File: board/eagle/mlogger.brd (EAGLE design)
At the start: 59.4 x 33.3 mm, 47 parts, among them J1 MICROSD-9P, SW1 SS-12D00G3, SW2 TVAF06-A020B-R, SW3 TVAF06-A020B-R

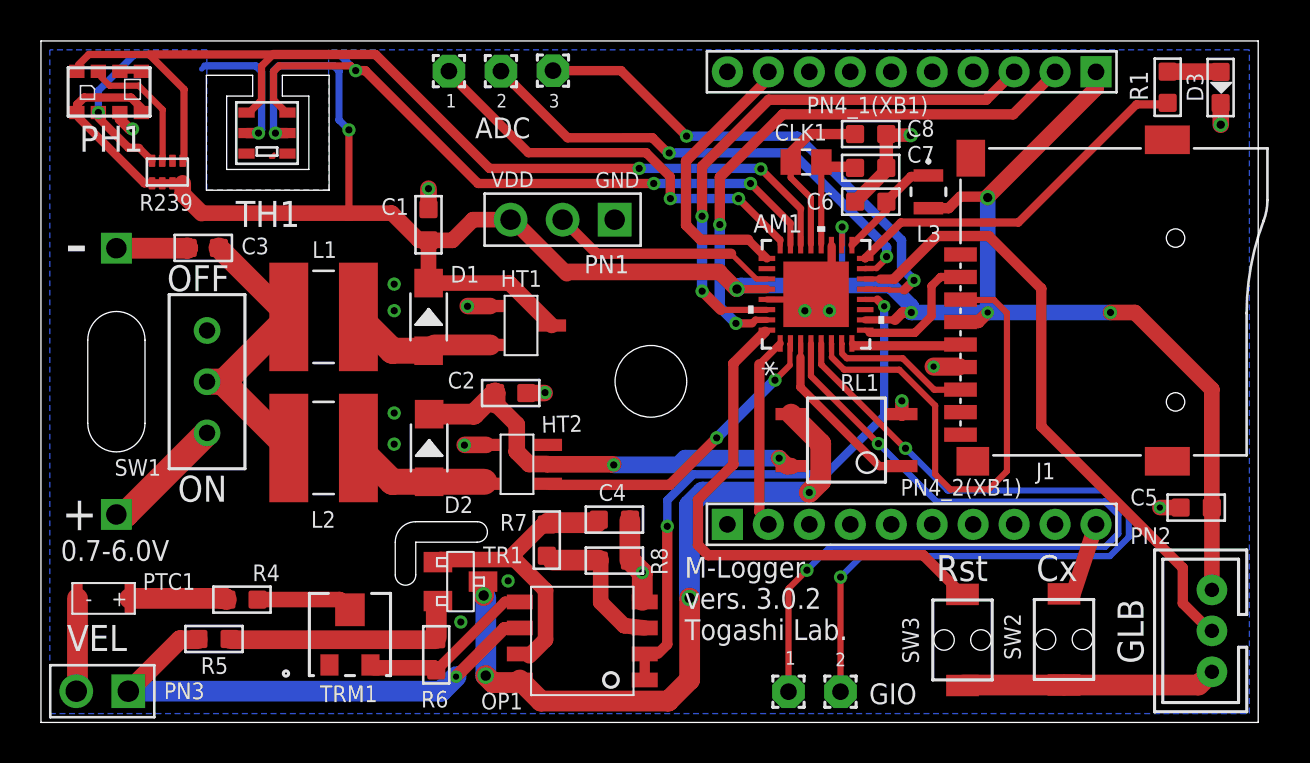
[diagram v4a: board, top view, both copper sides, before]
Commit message: 風速計配線ルート改善
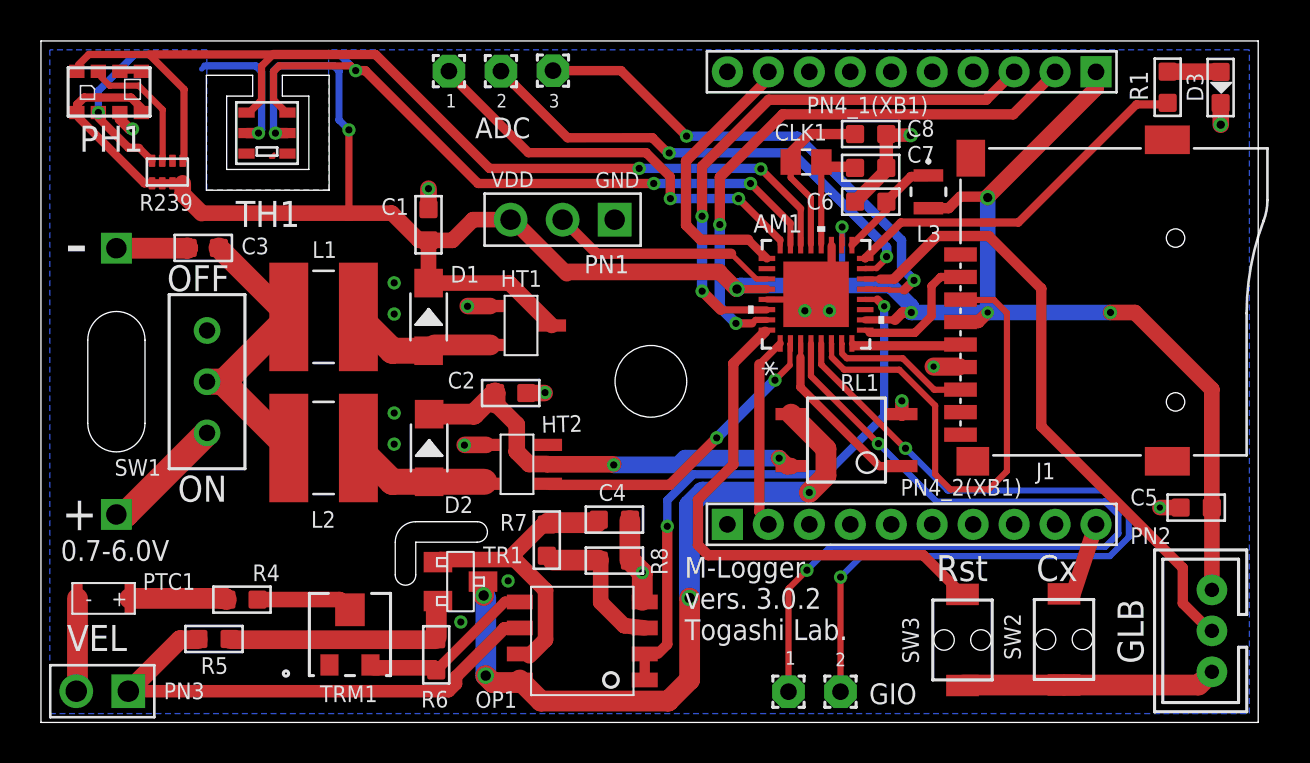
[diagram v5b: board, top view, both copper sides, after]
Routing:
- net P$1: track 24.9 -> 25.1 mm, vias 1 -> 0
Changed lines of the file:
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@@
 <element name="D2" library="Seeed-Diode" package="SOD-123" value="20V-1A" x="18.9546" y="13.4" smashed="yes" rot="R90">
 <attribute name="MPN" value="B5819W" x="18.9546" y="13.4" size="1.778" layer="27" rot="R90" display="off"/>
+<attribute name="NAME" x="19.5896" y="12.511" size="0.381" layer="33" ratio="10" rot="R90"/>
 <attribute name="NAME" x="19.6864" y="10.2246" size="0.8128" layer="25" ratio="11"/>
-<attribute name="NAME" x="19.5896" y="12.511" size="0.381" layer="33" ratio="10" rot="R90"/>
 <attribute name="VALUE" x="20.9866" y="11.495" size="0.889" layer="27" font="vector" ratio="11" rot="R90"/>
 </element>
@@
 </element>
 <element name="OP1" library="MyParts" package="NJM4565" value="NJM4565" x="29.4814" y="2.0724" smashed="yes" rot="R90">
-<attribute name="NAME" x="21.4874" y="0.6356" size="0.8128" layer="25"/>
+<attribute name="NAME" x="21.208" y="0.7118" size="0.8128" layer="25"/>
 </element>
 <element name="PTC1" library="MyParts" package="TFPT1206" value="TFPT1206" x="1.7832" y="6.055" smashed="yes">
@@
 <via x="22.8092" y="6.9088" extent="1-16" drill="0.35"/>
 <via x="17.2466" y="13.5866" extent="1-16" drill="0.35"/>
-<via x="17.2466" y="20.1042" extent="1-16" drill="0.35"/>
-<via x="17.2466" y="21.4004" extent="1-16" drill="0.35"/>
+<via x="17.2466" y="19.939" extent="1-16" drill="0.35"/>
+<via x="17.2466" y="21.463" extent="1-16" drill="0.35"/>
 <via x="37.3" y="20.1" extent="1-16" drill="0.35"/>
 <via x="38.5" y="20.1" extent="1-16" drill="0.35"/>
@@
 <wire x1="33.147" y1="24.3078" x2="33.147" y2="20.272" width="0.508" layer="16"/>
 <wire x1="33.147" y1="20.272" x2="33.9344" y2="19.4846" width="0.508" layer="16"/>
-<wire x1="34.8914" y1="19.6542" x2="34.7218" y2="19.4846" width="0.3556" layer="1"/>
+<wire x1="34.8914" y1="19.6542" x2="34.7218" y2="19.4846" width="0.3048" layer="1"/>
 <wire x1="33.9344" y1="19.4846" x2="34.7218" y2="19.4846" width="0.4064" layer="1"/>
 <wire x1="34.8914" y1="19.6542" x2="35.4457" y2="19.6542" width="0.3048" layer="1"/>
@@
 <via x="32.2834" y="21.0566" extent="1-16" drill="0.35"/>
 <wire x1="35.4457" y1="20.1542" x2="35.4337" y2="20.1422" width="0.254" layer="1"/>
-<wire x1="35.4337" y1="20.1422" x2="33.1978" y2="20.1422" width="0.3048" layer="1"/>
+<wire x1="35.4337" y1="20.1422" x2="33.1978" y2="20.1422" width="0.3556" layer="1"/>
 <wire x1="33.1978" y1="20.1422" x2="32.2834" y2="21.0566" width="0.508" layer="1"/>
 <wire x1="35.5346" y1="30.4038" x2="32.2806" y2="27.1498" width="0.508" layer="1"/>
@@
 <wire x1="22.6314" y1="4.5974" x2="23.3666625" y2="4.5974" width="0.6096" layer="1"/>
 <wire x1="20.2692" y1="2.2352" x2="22.6314" y2="4.5974" width="0.6096" layer="1"/>
-<wire x1="19.558" y1="1.524" x2="20.2692" y2="2.2352" width="1.016" layer="16"/>
-<wire x1="4.264" y1="1.524" x2="19.558" y2="1.524" width="1.016" layer="16"/>
 <wire x1="23.3666625" y1="4.5974" x2="23.3814" y2="4.6124" width="0.254" layer="1"/>
-<via x="20.2692" y="2.2352" extent="1-16" drill="0.3048"/>
+<wire x1="4.264" y1="1.524" x2="19.9136" y2="1.524" width="0.6096" layer="1"/>
+<wire x1="20.2692" y1="1.8796" x2="20.2692" y2="2.2352" width="0.6096" layer="1"/>
+<wire x1="20.2692" y1="1.8796" x2="19.9136" y2="1.524" width="0.6096" layer="1"/>
 </signal>
 <signal name="P$10" class="2">
@@
 <wire x1="21.6154" y1="6.1976" x2="21.6154" y2="6.8446" width="1.016" layer="1"/>
 <wire x1="21.6154" y1="6.8446" x2="21.584" y2="6.876" width="0.254" layer="1"/>
-<wire x1="36.6334" y1="15.0544" x2="38.0746" y2="13.6132" width="1.016" layer="1"/>
-<wire x1="38.0746" y1="13.6132" x2="38.0746" y2="11.7856" width="1.016" layer="1"/>
-<wire x1="38.0746" y1="11.7856" x2="37.5158" y2="11.2268" width="1.016" layer="1"/>
+<wire x1="36.6334" y1="15.0544" x2="38.3286" y2="13.3592" width="1.016" layer="1"/>
+<wire x1="38.3286" y1="13.3592" x2="38.3286" y2="12.0396" width="1.016" layer="1"/>
+<wire x1="38.3286" y1="12.0396" x2="37.5158" y2="11.2268" width="1.016" layer="1"/>
 <via x="37.5158" y="11.2268" extent="1-16" drill="0.35"/>
 <via x="31.6738" y="6.0706" extent="1-16" drill="0.508"/>
